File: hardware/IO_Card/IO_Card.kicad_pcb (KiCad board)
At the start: 2 copper layers, 79.5 x 99.9 mm, 18 parts, among them J1 6502 Edge, J2 6502 Pinheader, J3 Port A, J4 Port B, J7 Port A, J8 Port B, J9 VIA IO Select, U1 W65C22NxP, U2 W65C22NxP

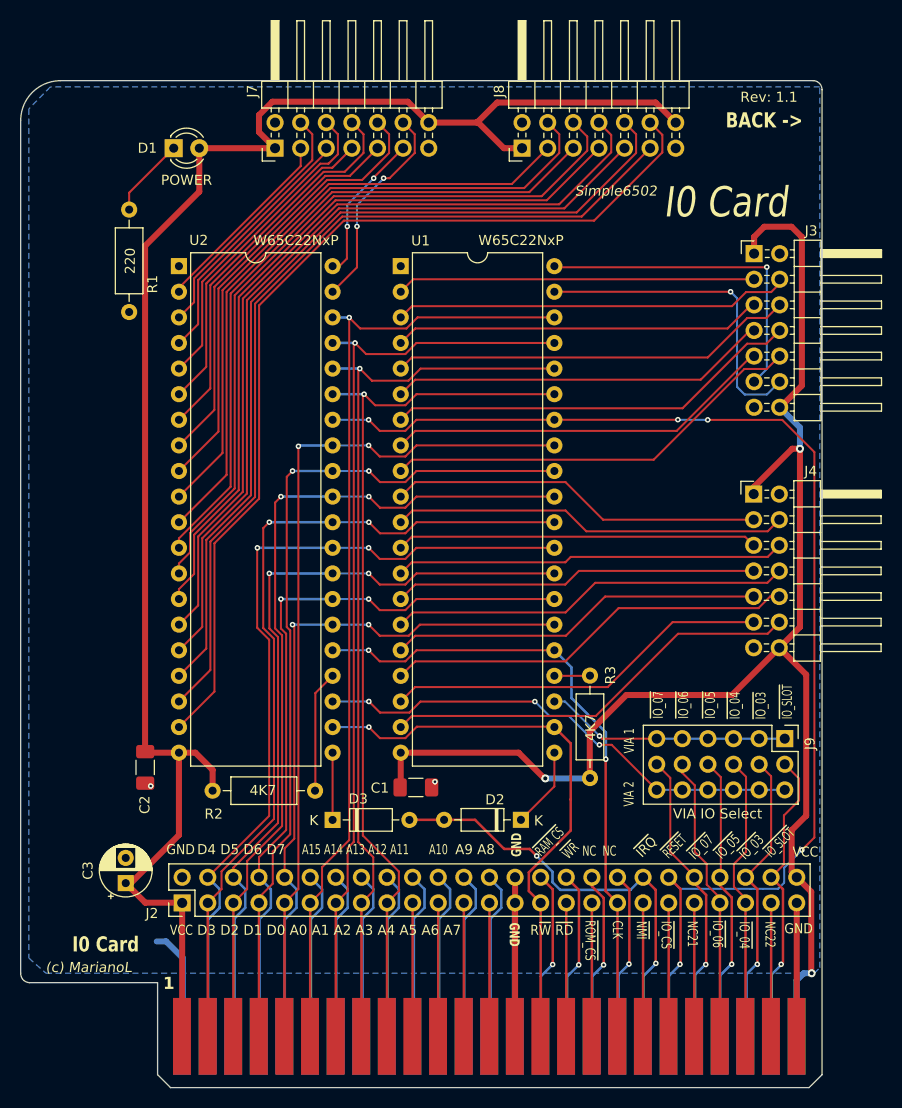
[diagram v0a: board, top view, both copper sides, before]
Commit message: Updated to Kicad 10 - IO Card added a PS2 port
multiple model and footprint updates
PS/2 via PIC added to the IO card
Project updated to Kicad 10
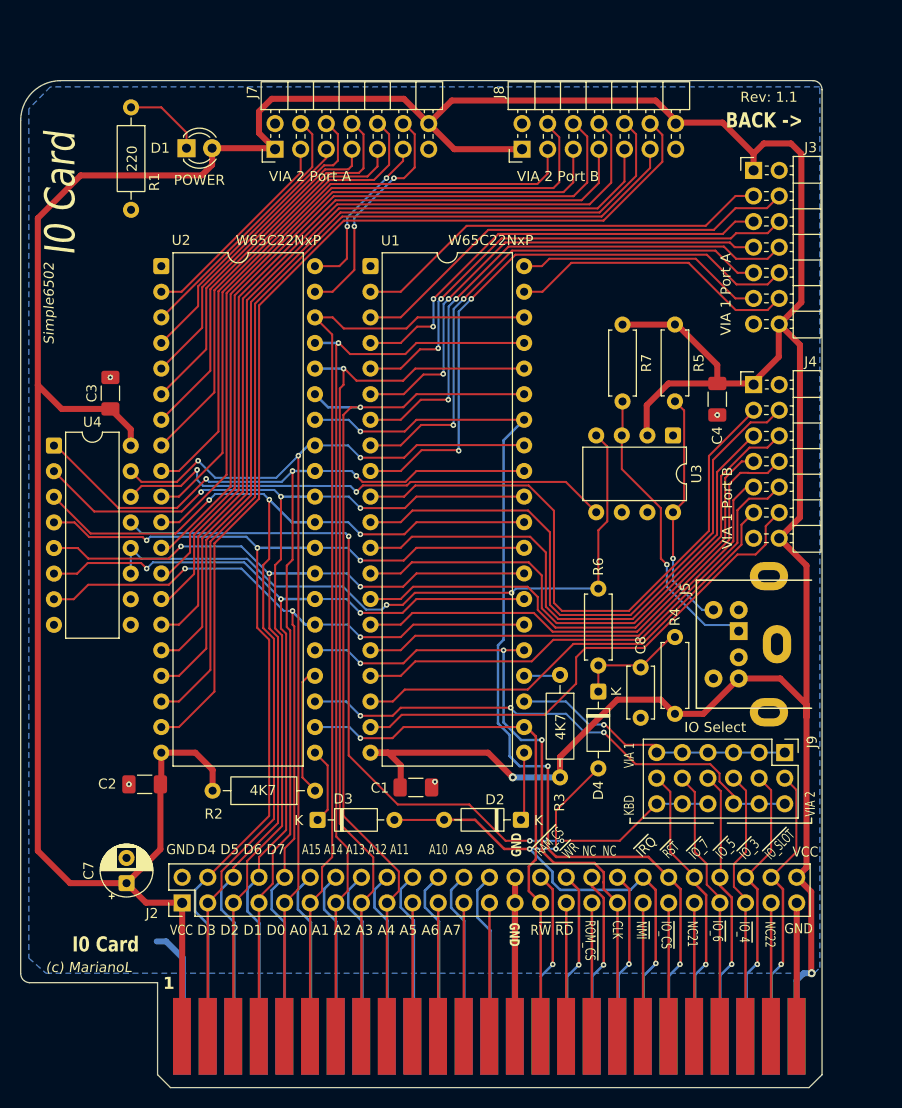
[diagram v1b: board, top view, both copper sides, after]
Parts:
- added C4: .1uF, Capacitor_SMD:C_1206_3216Metric_Pad1.33x1.80mm_HandSolder, F.Cu at (109.4, 62.2)
- added C7: 1000uf, Capacitor_THT:CP_Radial_D5.0mm_P2.50mm, F.Cu at (50.8, 110.2)
- added C8: 4.7nF, Capacitor_THT:C_Disc_D5.0mm_W2.5mm_P5.00mm, F.Cu at (101.8, 88.8)
- added D4: 1N6263, Diode_THT:D_DO-35_SOD27_P7.62mm_Horizontal, F.Cu at (97.6, 91.2)
- added J5: Mini-DIN-6, 6502_Components:J_Mini-DIN-6-Shield, F.Cu at (120.0, 86.5)
- added R4: 10K, Resistor_THT:R_Axial_DIN0207_L6.3mm_D2.5mm_P7.62mm_Horizontal, F.Cu at (105.2, 85.8)
- added R5: 4K7, Resistor_THT:R_Axial_DIN0207_L6.3mm_D2.5mm_P7.62mm_Horizontal, F.Cu at (105.2, 54.8)
- added R6: 2K2, Resistor_THT:R_Axial_DIN0207_L6.3mm_D2.5mm_P7.62mm_Horizontal, F.Cu at (97.6, 88.6)
- added R7: 4K7, Resistor_THT:R_Axial_DIN0207_L6.3mm_D2.5mm_P7.62mm_Horizontal, F.Cu at (100.0, 54.8)
- added U3: PIC10F202-IP, Package_DIP:DIP-8_W7.62mm, F.Cu at (105.0, 65.8)
- added U4: 74HC595, Package_DIP:DIP-16_W7.62mm, F.Cu at (43.6, 66.8)
- C3: value 1000uf -> .1uF; footprint Capacitor_THT:CP_Radial_D5.0mm_P2.50mm -> Capacitor_SMD:C_1206_3216Metric_Pad1.33x1.80mm_HandSolder
- J1: value 6502 Edge -> 6502 Edge; footprint Connector_PCBEdge:BUS_EdgePCB_Apple_2 -> 6502_Components:BUS_EdgePCB_Apple_2
- J2: footprint Connector_PinHeader_2.54mm:PinHeader_2x25_P2.54mm_Vertical_Counter_Clockwise -> 6502_Components:PinHeader_2x25_P2.54mm_Vertical_CounterClockWise
- J3: value Port A -> VIA 1 Port A
- J4: value Port B -> VIA 1 Port B
- J7: value Port A -> VIA 2 Port A
- J8: value Port B -> VIA 2 Port B
- J9: value VIA IO Select -> IO Select; footprint Connector_PinHeader_2.54mm:PinHeader_3x06_P2.54mm_Vertical -> 6502_Components:PinHeader_3x06_P2.54mm_A_B_Vertical
- moved C3 48.6 mm to (49.2, 61.6)
- moved J4 10.9 mm to (113.0, 60.8)
- moved R1 10.1 mm to (51.2, 33.2)
- moved J3 8.26 mm to (113.0, 39.5)
- moved U1 3.00 mm to (75.0, 49.0)
- moved R3 2.97 mm to (93.8, 89.5)
- moved U2 1.75 mm to (54.2, 49.0)
- moved C2 1.68 mm to (52.6, 100.4), turned to 180 degrees
- moved D3 1.49 mm to (69.8, 103.9)
- moved J9 1.38 mm to (116.1, 97.2)
- moved D1 1.27 mm to (56.8, 37.3)
- moved J7 0.10 mm to (65.5, 37.4)
- moved J8 0.10 mm to (90.0, 37.4)
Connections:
- net /2CA1 renamed V2.CA1
- net /2CA2 renamed V2.CA2
- net /2CB1 renamed V2.CB1
- net /2CB2 renamed V2.CB2
- net /2PA0 renamed V2.PA0
- net /2PA1 renamed V2.PA1
- net /2PA2 renamed V2.PA2
- net /2PA3 renamed V2.PA3
- net /2PA4 renamed V2.PA4
- net /2PA5 renamed V2.PA5
- net /2PA6 renamed V2.PA6
- net /2PA7 renamed V2.PA7
- net /2PB0 renamed V2.PB0
- net /2PB1 renamed V2.PB1
- net /2PB2 renamed V2.PB2
- net /2PB3 renamed V2.PB3
- net /2PB4 renamed V2.PB4
- net /2PB5 renamed V2.PB5
- net /2PB6 renamed V2.PB6
- net /2PB7 renamed V2.PB7
- net /A0 renamed A0
- net /A1 renamed A1
- net /A10 renamed A10
- net /A11 renamed A11
- net /A12 renamed A12
- net /A13 renamed A13
- net /A14 renamed A14
- net /A15 renamed A15
- net /A2 renamed A2
- net /A3 renamed A3
- net /A4 renamed A4
- net /A5 renamed A5
- net /A6 renamed A6
- net /A7 renamed A7
- net /A8 renamed A8
- net /A9 renamed A9
- net /CA1 renamed V1.CA1
- net /CA2 renamed V1.CA2
- net /CB1 renamed V1.CB1
- net /CB2 renamed V1.CB2
- net /CLK renamed CLK
- net /D0 renamed D0
- net /D1 renamed D1
- net /D2 renamed D2
- net /D3 renamed D3
- net /D4 renamed D4
- net /D5 renamed D5
- net /D6 renamed D6
- net /D7 renamed D7
- net /NC21 renamed NC21
- net /NC24 renamed NC24
- net /NC33 renamed NC33
- net /NC34 renamed NC34
- net /PA0 renamed V1.PA0
- net /PA1 renamed V1.PA1
- net /PA2 renamed V1.PA2
- net /PA3 renamed V1.PA3
- net /PA4 renamed V1.PA4
- net /PA5 renamed V1.PA5
- net /PA6 renamed V1.PA6
- net /PA7 renamed V1.PA7
- net /PB0 renamed V1.PB0
- net /PB1 renamed V1.PB1
- net /PB2 renamed V1.PB2
- net /PB3 renamed V1.PB3
- net /PB4 renamed V1.PB4
- net /PB5 renamed V1.PB5
- net /PB6 renamed V1.PB6
- net /PB7 renamed V1.PB7
- net /R~{W} renamed R~{W}
- net /~{IO_03} renamed ~{IO_03}
- net /~{IO_04} renamed ~{IO_04}
- net /~{IO_05} renamed ~{IO_05}
- net /~{IO_06} renamed ~{IO_06}
- net /~{IO_07} renamed ~{IO_07}
- net /~{IO_CS} renamed ~{IO_CS}
- net /~{IO_SLOT} renamed ~{IO_SLOT}
- net /~{NMI} renamed ~{NMI}
- net /~{RAM_CS} renamed ~{RAM_CS}
- net /~{RD} renamed ~{RD}
- net /~{RESET} renamed ~{RESET}
- net /~{ROM_CS} renamed ~{ROM_CS}
- net /~{WR} renamed ~{WR}
- J9 pad 4b: ~{CS_V2} -> KBD_SEL
- J9 pad 5b: ~{CS_V2} -> KBD_SEL
- J9 pad 6b: ~{CS_V2} -> KBD_SEL
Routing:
- net VCC: track 317.8 -> 417.3 mm, vias 3 -> 2
- net KBD_SEL: track 0.00 -> 84.6 mm, vias 0 -> 3
- net CLK_PS2: track 0.00 -> 68.4 mm, vias 0 -> 2
- net SER_PS2: track 0.00 -> 50.5 mm, vias 0 -> 2
- net KBD_DATA: track 0.00 -> 29.2 mm, vias 0 -> 1
- net D7: track 69.2 -> 95.0 mm, vias 2 -> 3
- net D3: track 83.6 -> 108.6 mm, vias 2 -> 3
- net V1.PB0: track 37.2 -> 61.6 mm
- net D1: track 84.6 -> 109.0 mm, vias 2 -> 3
- net ~{RESET}: track 123.0 -> 98.9 mm, vias 5 -> 3
- net KBD_CLK: track 0.00 -> 23.8 mm, vias 0 -> 1
- net V1.PB1: track 39.4 -> 62.2 mm
- net D2: track 84.1 -> 106.4 mm, vias 2 -> 3
- net D6: track 73.7 -> 95.8 mm, vias 2 -> 3
- net D5: track 78.3 -> 98.8 mm, vias 2 -> 3
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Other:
- board text added: "KBD"
- board text added: "~{IO_3}"
- board text added: "~{IO_4}"
- board text added: "~{IO_5}"
- board text added: "~{IO_6}"
- board text added: "~{IO_7}"
- board text added: "~{RST}"
- board text removed: "~{RESET}"
